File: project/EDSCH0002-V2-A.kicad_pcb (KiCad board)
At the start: 4 copper layers, 114 x 48 mm, 84 parts, among them J1 PCIEXP_X16_EDGE_MOUNT_CONN, J3 DISPLAY_PORT_SINK, J4 HEADER_1x2, J5 HEADER_1x2, J6 HEADER_1x2, J7 HEADER_1x2, J8 HEADER_1x2, U1 PCIe_HALF_x4_Gen2_SN65LVPE504, U2 OSC_100MHz_LVPECL, U3 OSC_125MHz_LVPECL, U4 OSC_148.5MHz_LVPECL, U5 SY100EP57V

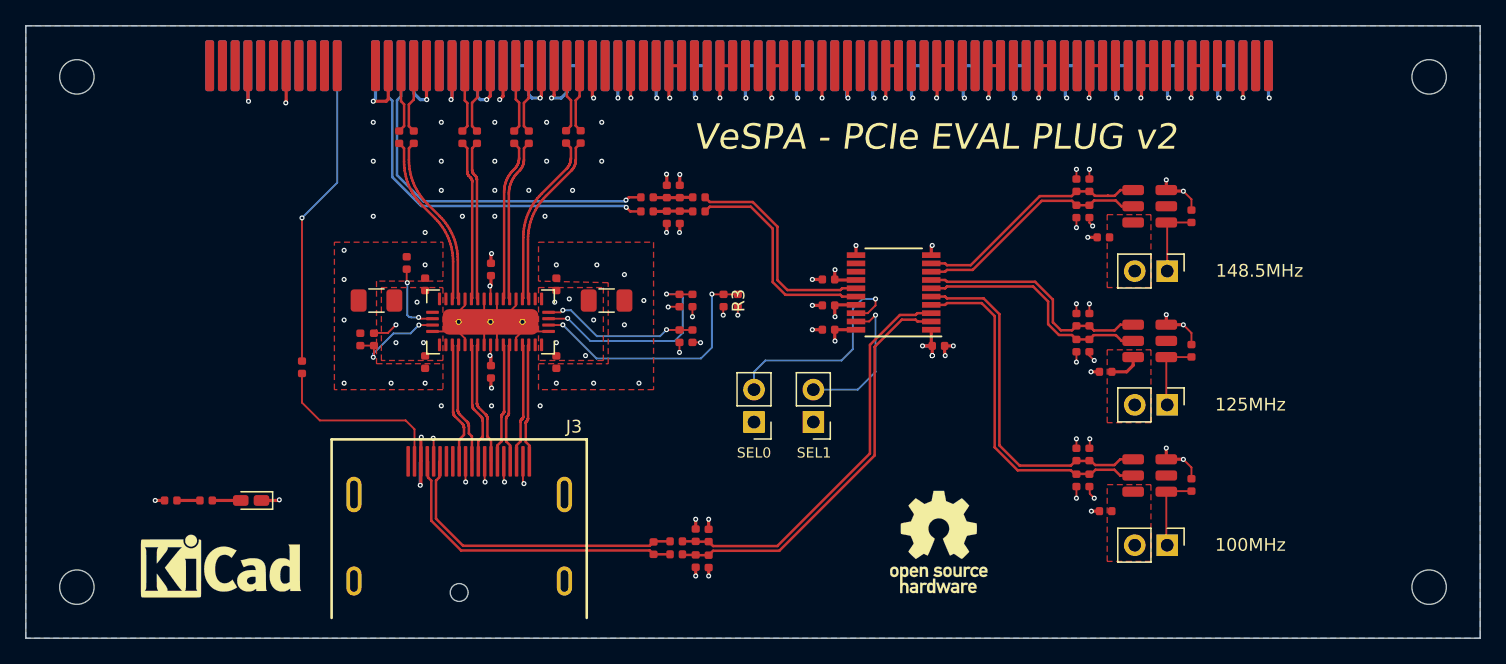
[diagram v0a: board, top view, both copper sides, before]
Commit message: Add gerber files
Panelized gerber included in hw-pcie-interposer are missing VCC plane.
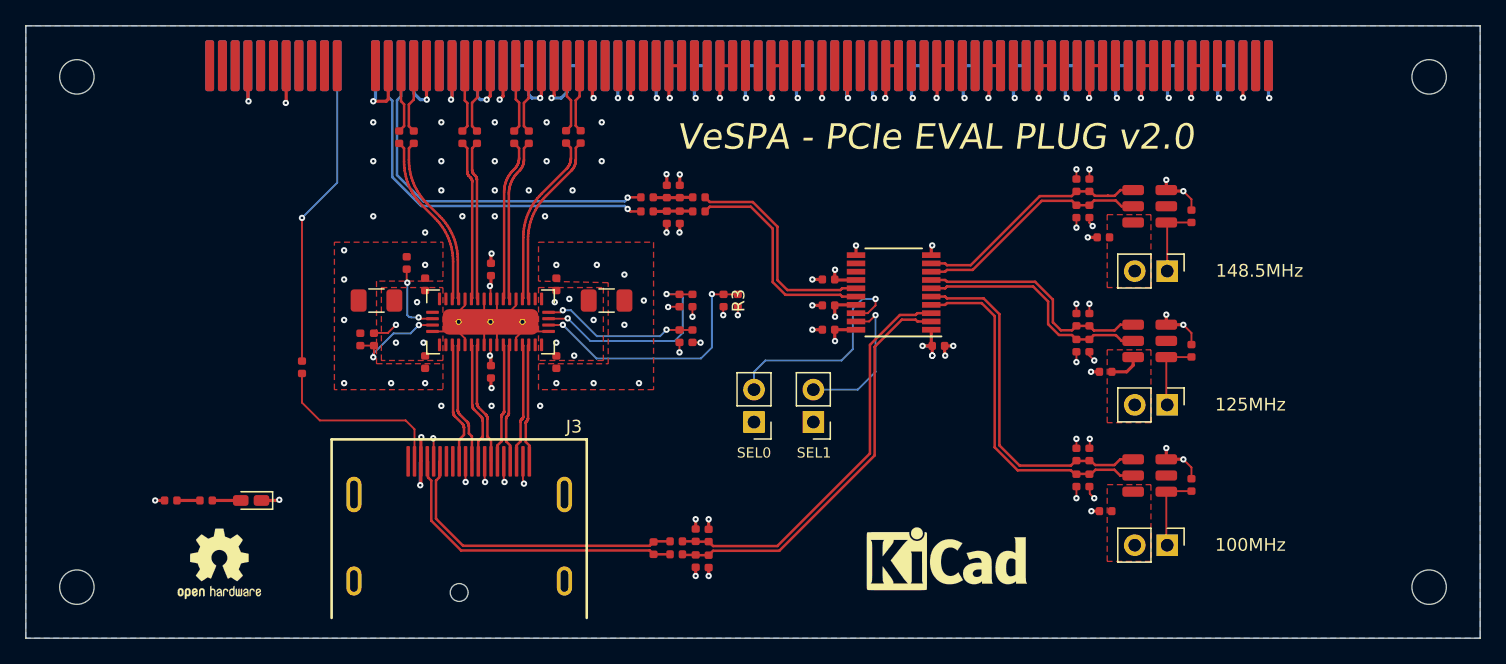
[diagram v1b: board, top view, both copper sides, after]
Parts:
- removed the REF** at (124.2, 81.2)
- added REF**: OSHW-Logo2_7.3x6mm_SilkScreen, Symbol:OSHW-Logo2_7.3x6mm_SilkScreen, F.Cu at (67.8, 82.9)
- moved REF** 56.9 mm to (124.8, 83.1)
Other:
- board text added: "VeSPA - PCIe EVAL PLUG v2.0"
- board text removed: "VeSPA - PCIe EVAL PLUG v2"
